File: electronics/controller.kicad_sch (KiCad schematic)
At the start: 0 parts

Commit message: cleaned code and folder structure, previous commit bug still remains
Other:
- title: (none) -> Controller Electronics
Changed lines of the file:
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@@
 	(paper "A4")
 	(title_block
+		(title "Controller Electronics")
 		(company "Ege Turan")
 		(comment 2 "Stanford, CA 94305")

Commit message: schematic progress with all current priority components and pin selections
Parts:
- added AE?: Antenna, symbol Device:Antenna
- added C11, C20, C? (x6): 0.1uF, symbol ME218_BaseLib:Cap
- added C?: 10uF, symbol ME218_BaseLib:Cap
- added J?: UART1, symbol Connector:Conn_01x02_Socket
- added M?: SG90 9g Micro Servo, symbol ME218_BaseLib:Motor_Servo
- added PRG?: MPLAB_Snap, symbol ME218_BaseLib:MPLAB_Snap
- added R10, R18, R? (x4): 10K, symbol ME218_BaseLib:Res2
- added R?: 1K, symbol ME218_BaseLib:Res2
- added RV1: 10K, symbol Device:R_Potentiometer
- added SW4, SW? (x2): Start, symbol ME218_BaseLib:SW-PB
- added SW7: SW_SPDT_LIMIT, symbol Switch:SW_SPDT_XKB_DMx-xxxx-1
- added SW?: SW_SPDT, symbol Switch:SW_SPDT
- added SW?: Reset, symbol ME218_BaseLib:SW-PB
- added U5: Joystick_2_Axis_1SW, symbol ME218_BaseLib:Joystick_2_Axis_1SW
- added U?: XBee_SMT, RF_Module:Digi_XBee_SMT, symbol RF_ZigBee:XBee_SMT
- added U?: PIC32MX170F256B, symbol ME218_BaseLib:PIC32MX170F256B
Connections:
- new net: AE?.1 (A), U?.36 (RF)
- new net: PRG?.1 (~{MCLR}/Vpp), R?.1, U?.1 (~{MCLR})
- new net: PRG?.4 (PGData), U?.4 (PGED1/RB0)
- new net: PRG?.5 (PGClk), U?.5 (PGEC1/RB1)
- new net: C?.2, U?.20 (Vcap)
- new net: C?.1, R?.1, R?.2, SW?.1
- new net +3V3: C?.1, C?.2, PRG?.2 (Vdd), R10.2, R18.2, R?.2, R?.2, R?.2, R?.2, RV1.1, U5.2 (Vcc), U?.13 (Vdd), U?.2 (VCC), U?.28 (AVdd)
- new net +5V: M?.2 (+)
- new net DriveRefuelSwitch: C?.1, R?.1, SW?.2 (B), U?.10 (RA3)
- new net FuelIndicatorPWM4: M?.1 (PWM), U?.9 (RA2)
- new net GND: C11.2, C20.2, C?.1, C?.1, C?.2, C?.2, C?.2, C?.2, C?.2, M?.3 (-), PRG?.3 (Vss), RV1.3, SW4.2, SW7.2 (B), SW?.2, SW?.2, SW?.2, SW?.3 (C), U5.1 (GND), U?.1 (GND), U?.11 (GND), U?.13 (GND), U?.19 (Vss), U?.22 (GND), U?.27 (AVss), U?.35 (GND), U?.8 (Vss)
- new net GateButton: C?.1, R?.1, SW?.1, U?.25 (RB14)
- new net JoystickDirectionADC: U5.4 (VRy), U?.3 (RA1)
- new net JoystickThurstADC: U5.3 (VRx), U?.2 (RA0)
- new net PairButton: C11.1, R10.1, SW4.1, U?.26 (RB15)
- new net RX: J?.1 (Pin_1), U?.16 (5VT/RB7)
- new net RefuelLimit: C20.1, R18.1, SW7.1 (A), U?.23 (RB12)
- new net SelectBoatADC: RV1.2, U?.6 (RB2)
- new net SprayButton: C?.1, R?.1, SW?.1, U?.24 (RB13)
- new net TX: J?.2 (Pin_2), U?.15 (PGEC3/5VT/RB6)
- new net UART2RX: U?.17 (5VT/RB8), U?.3 (DIO13/UART_TX)
- new net UART2TX: U?.18 (PGED2/5VT/RB9), U?.4 (DIO14/UART_RX/~{CONFIG})
- no-connect marks 0 -> 29
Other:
- note added: "for programming"

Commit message: added status leds to schematic
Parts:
- renumbered C20 to C?, C11 to C?, R10 to R?, R18 to R?, RV1 to RV?, SW7 to SW?, SW4 to SW?, U5 to U?
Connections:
- net StatusLED1: now reaches U?.11 (RB4)
- net StatusLED2: now reaches U?.12 (RA4)
- net StatusLED3: now reaches U?.14 (PGED3/5VT/RB5)
- no-connect marks 29 -> 26

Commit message: added water pump to RA4
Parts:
- gave numbers to parts that had none: 8
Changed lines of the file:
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@@
 		(dnp no)
 		(fields_autoplaced yes)
-		(property "Reference" "#PWR?"
+		(property "Reference" "#PWR0102"
 			(at 189.484 179.07 0)
 			(effects
@@
 		(dnp no)
 		(fields_autoplaced yes)
-		(property "Reference" "#PWR?"
+		(property "Reference" "#PWR041"
 			(at 90.17 182.88 0)
 			(effects
@@
 		(dnp no)
 		(fields_autoplaced yes)
-		(property "Reference" "R?"
+		(property "Reference" "R10"
 			(at 238.76 128.2699 0)
 			(effects
@@
 		(dnp no)
 		(fields_autoplaced yes)
-		(property "Reference" "#PWR?"
+		(property "Reference" "#PWR06"
 			(at 67.31 109.22 0)
 			(effects
@@
 		(on_board yes)
 		(dnp no)
-		(property "Reference" "SW?"
+		(property "Reference" "SW7"
 			(at 182.88 161.544 0)
 			(effects
@@
 		(dnp no)
 		(fields_autoplaced yes)
-		(property "Reference" "#PWR?"
+		(property "Reference" "#PWR044"
 			(at 248.92 210.82 0)
 			(effects
@@
 		(dnp no)
 		(fields_autoplaced yes)
-		(property "Reference" "#PWR?"
+		(property "Reference" "#PWR039"
 			(at 236.22 163.83 0)
 			(effects
@@
 		(dnp no)
 		(fields_autoplaced yes)
-		(property "Reference" "C?"
+		(property "Reference" "C20"
 			(at 167.64 171.4499 0)
 			(effects
@@
 		(dnp no)
 		(fields_autoplaced yes)
-		(property "Reference" "#PWR?"
+		(property "Reference" "#PWR05"
 			(at 53.34 99.06 0)
 			(effects
@@
 		(dnp no)
 		(fields_autoplaced yes)
-		(property "Reference" "#PWR?"
+		(property "Reference" "#PWR034"
 			(at 163.83 129.54 0)
 			(effects
@@
 		(dnp no)
 		(fields_autoplaced yes)
-		(property "Reference" "SW?"
+		(property "Reference" "SW4"
 			(at 252.73 134.6199 90)
 			(effects
@@
 		(dnp no)
 		(fields_autoplaced yes)
-		(property "Reference" "#PWR?"
+		(property "Reference" "#PWR031"
 			(at 36.83 138.43 0)
 			(effects
@@
 		(dnp no)
 		(fields_autoplaced yes)
-		(property "Reference" "#PWR?"
+		(property "Reference" "#PWR036"
 			(at 190.5 143.51 0)
 			(effects
@@
 		(dnp no)
 		(fields_autoplaced yes)
-		(property "Reference" "#PWR?"
+		(property "Reference" "#PWR029"
 			(at 228.6 41.91 0)
 			(effects
@@
 		(dnp no)
 		(fields_autoplaced yes)
-		(property "Reference" "#PWR?"
+		(property "Reference" "#PWR04"
 			(at 53.34 88.9 0)
 			(effects
@@
 		(dnp no)
 		(fields_autoplaced yes)
-		(property "Reference" "#PWR?"
+		(property "Reference" "#PWR07"
 			(at 100.33 37.084 0)
 			(effects
@@
 		(dnp no)
 		(fields_autoplaced yes)
-		(property "Reference" "#PWR?"
+		(property "Reference" "#PWR042"
 			(at 248.92 181.61 0)
 			(effects
@@
 		(dnp no)
 		(fields_autoplaced yes)
-		(property "Reference" "RV?"
+		(property "Reference" "RV1"
 			(at 34.29 167.6399 0)
 			(effects
@@
 		(dnp no)
 		(fields_autoplaced yes)
-		(property "Reference" "#PWR?"
+		(property "Reference" "#PWR012"
 			(at 129.54 71.12 0)
 			(effects
@@
 		(dnp no)
 		(fields_autoplaced yes)
-		(property "Reference" "#PWR?"
+		(property "Reference" "#PWR040"
 			(at 90.17 165.1 0)
 			(effects
@@
 		(dnp no)
 		(fields_autoplaced yes)
-		(property "Reference" "#PWR?"
+		(property "Reference" "#PWR030"
 			(at 228.6 104.14 0)
 			(effects
@@
 		(dnp no)
 		(fields_autoplaced yes)
-		(property "Reference" "#PWR?"
+		(property "Reference" "#PWR0100"
 			(at 163.83 165.1 0)
 			(effects
@@
 		(dnp no)
 		(fields_autoplaced yes)
-		(property "Reference" "#PWR?"
+		(property "Reference" "#PWR08"
 			(at 113.03 54.864 0)
 			(effects
@@
 		(dnp no)
 		(fields_autoplaced yes)
-		(property "Reference" "#PWR?"
+		(property "Reference" "#PWR09"
 			(at 36.83 130.81 0)
 			(effects
@@
 		(dnp no)
 		(fields_autoplaced yes)
-		(property "Reference" "#PWR?"
+		(property "Reference" "#PWR037"
 			(at 236.22 129.54 0)
 			(effects
@@
 		(dnp no)
 		(fields_autoplaced yes)
-		(property "Reference" "#PWR?"
+		(property "Reference" "#PWR033"
 			(at 36.83 179.07 0)
 			(effects
@@
 		(dnp no)
 		(fields_autoplaced yes)
-		(property "Reference" "#PWR?"
+		(property "Reference" "#PWR043"
 			(at 236.22 193.04 0)
 			(effects
@@
 		(dnp no)
 		(fields_autoplaced yes)
-		(property "Reference" "R?"
+		(property "Reference" "R18"
 			(at 166.37 163.8299 0)
 			(effects
@@
 		(dnp no)
 		(fields_autoplaced yes)
-		(property "Reference" "#PWR?"
+		(property "Reference" "#PWR032"
 			(at 36.83 168.91 0)
 			(effects
@@
 		(dnp no)
 		(fields_autoplaced yes)
-		(property "Reference" "C?"
+		(property "Reference" "C11"
 			(at 240.03 135.8899 0)
 			(effects
@@
 		(dnp no)
 		(fields_autoplaced yes)
-		(property "Reference" "#PWR?"
+		(property "Reference" "#PWR0101"
 			(at 163.83 182.88 0)
 			(effects
@@
 		(dnp no)
 		(fields_autoplaced yes)
-		(property "Reference" "#PWR?"
+		(property "Reference" "#PWR038"
 			(at 248.92 147.32 0)
 			(effects
@@
 		(dnp no)
 		(fields_autoplaced yes)
-		(property "Reference" "#PWR?"
+		(property "Reference" "#PWR01"
 			(at 53.34 52.07 0)
 			(effects
@@
 		(dnp no)
 		(fields_autoplaced yes)
-		(property "Reference" "#PWR?"
+		(property "Reference" "#PWR035"
 			(at 163.83 147.32 0)
 			(effects
@@
 		(dnp no)
 		(fields_autoplaced yes)
-		(property "Reference" "#PWR?"
+		(property "Reference" "#PWR010"
 			(at 129.54 49.53 0)
 			(effects
@@
 		(dnp no)
 		(fields_autoplaced yes)
-		(property "Reference" "U?"
+		(property "Reference" "U5"
 			(at 114.3 167.6399 0)
 			(effects
@@
 		(dnp no)
 		(fields_autoplaced yes)
-		(property "Reference" "#PWR?"
+		(property "Reference" "#PWR03"
 			(at 53.34 62.23 0)
 			(effects

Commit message: water pump schematic updated to be driven by IRLZ34N N-channel MOSFET
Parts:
- gave numbers to parts that had none: 22
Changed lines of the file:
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@@
 		(dnp no)
 		(fields_autoplaced yes)
-		(property "Reference" "SW?"
+		(property "Reference" "SW5"
 			(at 252.73 168.9099 90)
 			(effects
@@
 			(project "boatElectronics"
 				(path "/bd24c4db-4e36-4117-bd4f-5228ef241da9/ebf9c9fd-19f1-445b-9c7b-2cb236965a45"
-					(reference "SW?")
+					(reference "SW5")
 					(unit 1)
 				)
@@
 		(dnp no)
 		(fields_autoplaced yes)
-		(property "Reference" "SW?"
+		(property "Reference" "SW3"
 			(at 184.15 124.46 0)
 			(effects
@@
 			(project ""
 				(path "/bd24c4db-4e36-4117-bd4f-5228ef241da9/ebf9c9fd-19f1-445b-9c7b-2cb236965a45"
-					(reference "SW?")
+					(reference "SW3")
 					(unit 1)
 				)
@@
 		(dnp no)
 		(fields_autoplaced yes)
-		(property "Reference" "U?"
+		(property "Reference" "U4"
 			(at 233.2833 39.37 0)
 			(effects
@@
 			(project "boatElectronics"
 				(path "/bd24c4db-4e36-4117-bd4f-5228ef241da9/ebf9c9fd-19f1-445b-9c7b-2cb236965a45"
-					(reference "U?")
+					(reference "U4")
 					(unit 1)
 				)
@@
 		(dnp no)
 		(fields_autoplaced yes)
-		(property "Reference" "PRG?"
+		(property "Reference" "PRG1"
 			(at 152.4 53.3399 0)
 			(effects
@@
 			(project "boatElectronics"
 				(path "/bd24c4db-4e36-4117-bd4f-5228ef241da9/ebf9c9fd-19f1-445b-9c7b-2cb236965a45"
-					(reference "PRG?")
+					(reference "PRG1")
 					(unit 1)
 				)
@@
 		(on_board yes)
 		(dnp no)
-		(property "Reference" "C?"
+		(property "Reference" "C3"
 			(at 74.422 104.902 90)
 			(effects
@@
 			(project "boatElectronics"
 				(path "/bd24c4db-4e36-4117-bd4f-5228ef241da9/ebf9c9fd-19f1-445b-9c7b-2cb236965a45"
-					(reference "C?")
+					(reference "C3")
 					(unit 1)
 				)
@@
 		(on_board yes)
 		(dnp no)
-		(property "Reference" "J?"
+		(property "Reference" "J4"
 			(at 110.49 72.3899 0)
 			(effects
@@
 			(project "boatElectronics"
 				(path "/bd24c4db-4e36-4117-bd4f-5228ef241da9/ebf9c9fd-19f1-445b-9c7b-2cb236965a45"
-					(reference "J?")
+					(reference "J4")
 					(unit 1)
 				)
@@
 		(on_board yes)
 		(dnp no)
-		(property "Reference" "C?"
+		(property "Reference" "C1"
 			(at 45.212 50.546 0)
 			(effects
@@
 			(project "boatElectronics"
 				(path "/bd24c4db-4e36-4117-bd4f-5228ef241da9/ebf9c9fd-19f1-445b-9c7b-2cb236965a45"
-					(reference "C?")
+					(reference "C1")
 					(unit 1)
 				)
@@
 		(dnp no)
 		(fields_autoplaced yes)
-		(property "Reference" "AE?"
+		(property "Reference" "AE2"
 			(at 267.97 66.0399 90)
 			(effects
@@
 			(project "boatElectronics"
 				(path "/bd24c4db-4e36-4117-bd4f-5228ef241da9/ebf9c9fd-19f1-445b-9c7b-2cb236965a45"
-					(reference "AE?")
+					(reference "AE2")
 					(unit 1)
 				)
@@
 		(dnp no)
 		(fields_autoplaced yes)
-		(property "Reference" "R?"
+		(property "Reference" "R3"
 			(at 166.37 128.2699 0)
 			(effects
@@
 			(project "boatElectronics"
 				(path "/bd24c4db-4e36-4117-bd4f-5228ef241da9/ebf9c9fd-19f1-445b-9c7b-2cb236965a45"
-					(reference "R?")
+					(reference "R3")
 					(unit 1)
 				)
@@
 		(dnp no)
 		(fields_autoplaced yes)
-		(property "Reference" "M?"
+		(property "Reference" "M2"
 			(at 82.55 126.5668 0)
 			(effects
@@
 			(project "boatElectronics"
 				(path "/bd24c4db-4e36-4117-bd4f-5228ef241da9/ebf9c9fd-19f1-445b-9c7b-2cb236965a45"
-					(reference "M?")
+					(reference "M2")
 					(unit 1)
 				)
@@
 		(dnp no)
 		(fields_autoplaced yes)
-		(property "Reference" "R?"
+		(property "Reference" "R1"
 			(at 96.52 34.544 90)
 			(effects
@@
 			(project "boatElectronics"
 				(path "/bd24c4db-4e36-4117-bd4f-5228ef241da9/ebf9c9fd-19f1-445b-9c7b-2cb236965a45"
-					(reference "R?")
+					(reference "R1")
 					(unit 1)
 				)
@@
 		(dnp no)
 		(fields_autoplaced yes)
-		(property "Reference" "U?"
+		(property "Reference" "U3"
 			(at 73.025 40.64 0)
 			(effects
@@
 			(project "boatElectronics"
 				(path "/bd24c4db-4e36-4117-bd4f-5228ef241da9/ebf9c9fd-19f1-445b-9c7b-2cb236965a45"
-					(reference "U?")
+					(reference "U3")
 					(unit 1)
 				)
@@
 		(dnp no)
 		(fields_autoplaced yes)
-		(property "Reference" "R?"
+		(property "Reference" "R6"
 			(at 238.76 162.5599 0)
 			(effects
@@
 			(project "boatElectronics"
 				(path "/bd24c4db-4e36-4117-bd4f-5228ef241da9/ebf9c9fd-19f1-445b-9c7b-2cb236965a45"
-					(reference "R?")
+					(reference "R6")
 					(unit 1)
 				)
@@
 		(dnp no)
 		(fields_autoplaced yes)
-		(property "Reference" "SW?"
+		(property "Reference" "SW6"
 			(at 252.73 198.1199 90)
 			(effects
@@
 			(project "boatElectronics"
 				(path "/bd24c4db-4e36-4117-bd4f-5228ef241da9/ebf9c9fd-19f1-445b-9c7b-2cb236965a45"
-					(reference "SW?")
+					(reference "SW6")
 					(unit 1)
 				)
@@
 		(dnp no)
 		(fields_autoplaced yes)
-		(property "Reference" "C?"
+		(property "Reference" "C10"
 			(at 240.03 170.1799 0)
 			(effects
@@
 			(project "boatElectronics"
 				(path "/bd24c4db-4e36-4117-bd4f-5228ef241da9/ebf9c9fd-19f1-445b-9c7b-2cb236965a45"
-					(reference "C?")
+					(reference "C10")
 					(unit 1)
 				)
@@
 		(dnp no)
 		(fields_autoplaced yes)
-		(property "Reference" "R?"
+		(property "Reference" "R2"
 			(at 102.87 35.8139 0)
 			(effects
@@
 			(project "boatElectronics"
 				(path "/bd24c4db-4e36-4117-bd4f-5228ef241da9/ebf9c9fd-19f1-445b-9c7b-2cb236965a45"
-					(reference "R?")
+					(reference "R2")
 					(unit 1)
 				)
@@
 		(dnp no)
 		(fields_autoplaced yes)
-		(property "Reference" "C?"
+		(property "Reference" "C9"
 			(at 167.64 135.8899 0)
 			(effects
@@
 			(project "boatElectronics"
 				(path "/bd24c4db-4e36-4117-bd4f-5228ef241da9/ebf9c9fd-19f1-445b-9c7b-2cb236965a45"
-					(reference "C?")
+					(reference "C9")
 					(unit 1)
 				)
@@
 		(dnp no)
 		(fields_autoplaced yes)
-		(property "Reference" "C?"
+		(property "Reference" "C4"
 			(at 104.14 43.4339 0)
 			(effects
@@
 			(project "boatElectronics"
 				(path "/bd24c4db-4e36-4117-bd4f-5228ef241da9/ebf9c9fd-19f1-445b-9c7b-2cb236965a45"
-					(reference "C?")
+					(reference "C4")
 					(unit 1)
 				)
@@
 		(dnp no)
 		(fields_autoplaced yes)
-		(property "Reference" "R?"
+		(property "Reference" "R8"
 			(at 238.76 191.7699 0)
 			(effects
@@
 			(project "boatElectronics"
 				(path "/bd24c4db-4e36-4117-bd4f-5228ef241da9/ebf9c9fd-19f1-445b-9c7b-2cb236965a45"
-					(reference "R?")
+					(reference "R8")
 					(unit 1)
 				)
@@
 		(dnp no)
 		(fields_autoplaced yes)
-		(property "Reference" "C?"
+		(property "Reference" "C12"
 			(at 240.03 199.3899 0)
 			(effects
@@
 			(project "boatElectronics"
 				(path "/bd24c4db-4e36-4117-bd4f-5228ef241da9/ebf9c9fd-19f1-445b-9c7b-2cb236965a45"
-					(reference "C?")
+					(reference "C12")
 					(unit 1)
 				)
@@
 		(on_board yes)
 		(dnp no)
-		(property "Reference" "C?"
+		(property "Reference" "C2"
 			(at 46.736 87.376 0)
 			(effects
@@
 			(project "boatElectronics"
 				(path "/bd24c4db-4e36-4117-bd4f-5228ef241da9/ebf9c9fd-19f1-445b-9c7b-2cb236965a45"
-					(reference "C?")
+					(reference "C2")
 					(unit 1)
 				)
@@
 		(dnp no)
 		(fields_autoplaced yes)
-		(property "Reference" "SW?"
+		(property "Reference" "SW2"
 			(at 116.84 42.1639 90)
 			(effects
@@
 			(project "boatElectronics"
 				(path "/bd24c4db-4e36-4117-bd4f-5228ef241da9/ebf9c9fd-19f1-445b-9c7b-2cb236965a45"
-					(reference "SW?")
+					(reference "SW2")
 					(unit 1)
 				)

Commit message: rearrange schematic
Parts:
- removed C12: 0.1uF, symbol ME218_BaseLib:Cap
- removed R8: 10K, symbol ME218_BaseLib:Res2
- removed SW6: Start, symbol ME218_BaseLib:SW-PB
- SW5: value Start -> Spray

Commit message: update and reorganize electronics for documentation
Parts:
- removed C10, C11, C20, C9: 0.1uF, symbol ME218_BaseLib:Cap
- removed R10, R18, R3, R6: 10K, symbol ME218_BaseLib:Res2
- removed SW3: SW_SPDT, symbol Switch:SW_SPDT
- added D1, D2, D3: LED, symbol Device:LED
- added R5, R6, R7: 220, symbol Device:R
- SW4: value Start -> Pair
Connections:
- net GND: now also R5.2, R6.2, R7.2
- net StatusLED1: now also D1.2 (A)
- net StatusLED2: now also D2.2 (A)
- net StatusLED3: now also D3.2 (A)
- net DriveRefuelSwitch: no longer names the net of U3.10 (RA3)
- new net: D3.1 (K), R6.1
- new net: D2.1 (K), R5.1
- new net: D1.1 (K), R7.1
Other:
- note added: "Using internal pull-up"
- moved on the sheet: SW4, SW5

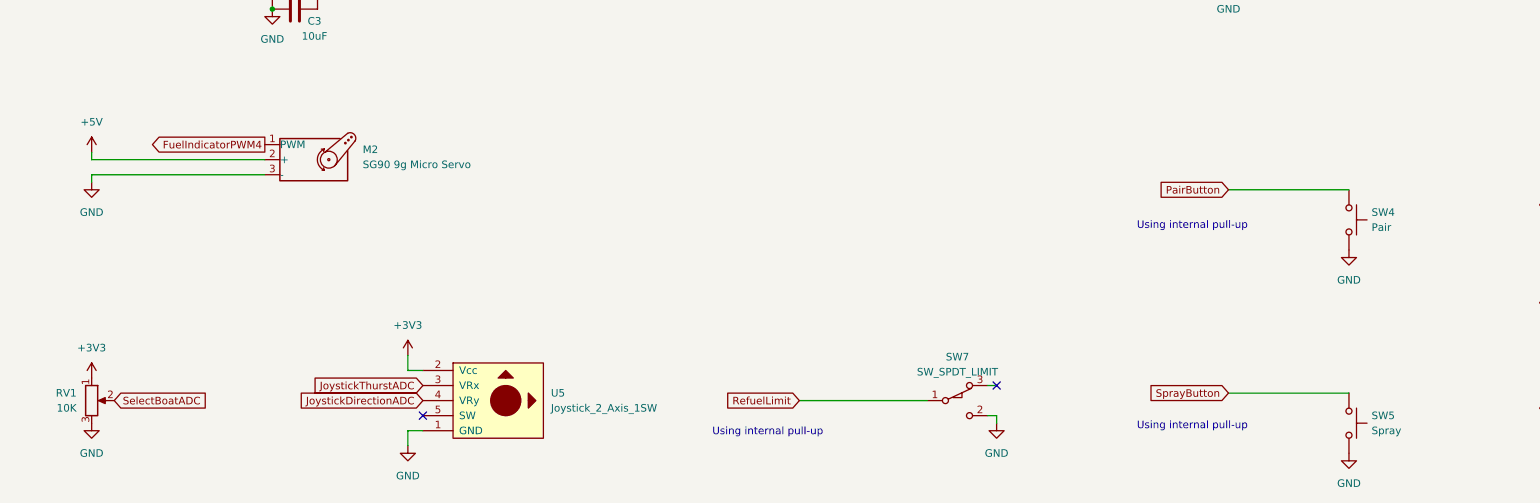
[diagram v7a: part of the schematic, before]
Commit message: update controller schematic to match future-proofing
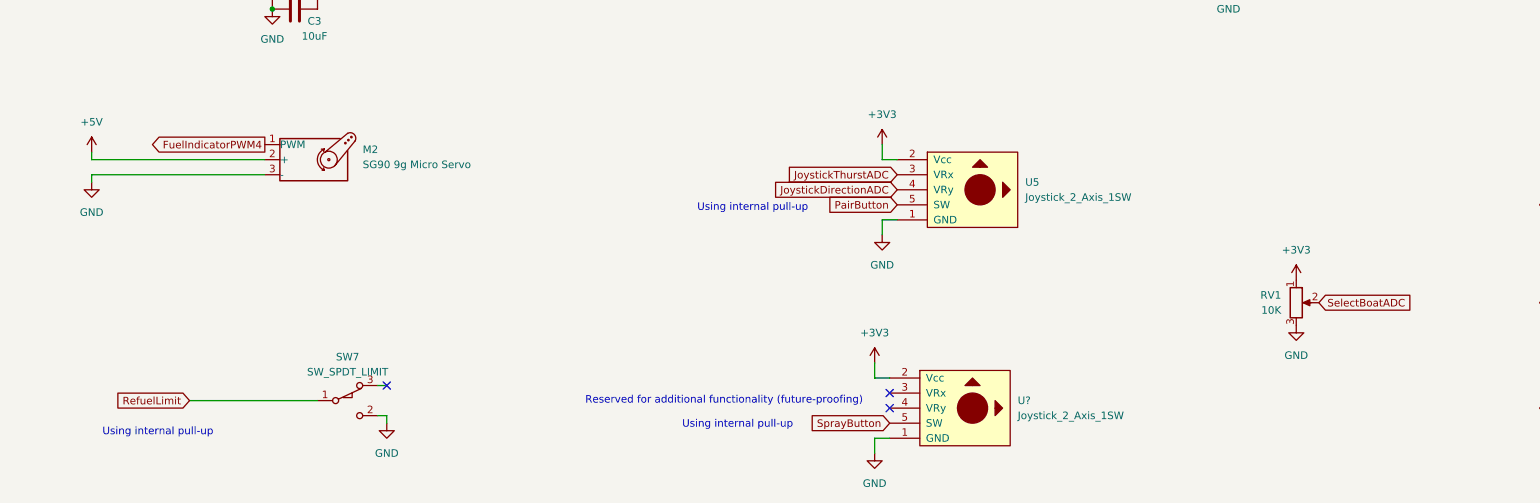
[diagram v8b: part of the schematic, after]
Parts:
- removed SW4: Pair, symbol ME218_BaseLib:SW-PB
- removed SW5: Spray, symbol ME218_BaseLib:SW-PB
- added U?: Joystick_2_Axis_1SW, symbol ME218_BaseLib:Joystick_2_Axis_1SW
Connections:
- net +3V3: now also U?.2 (Vcc)
- net GND: now also U?.1 (GND)
- net PairButton: now also U5.5 (SW)
- net SprayButton: now also U?.5 (SW)
- no-connect marks 26 -> 27
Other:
- note added: "Reserved for additional functionality (future-proofing)"
- moved on the sheet: RV1, SW7, U5
